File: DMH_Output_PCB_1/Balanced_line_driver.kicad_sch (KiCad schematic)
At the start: 12 parts, among them U10 NE5532, U9 NE5532

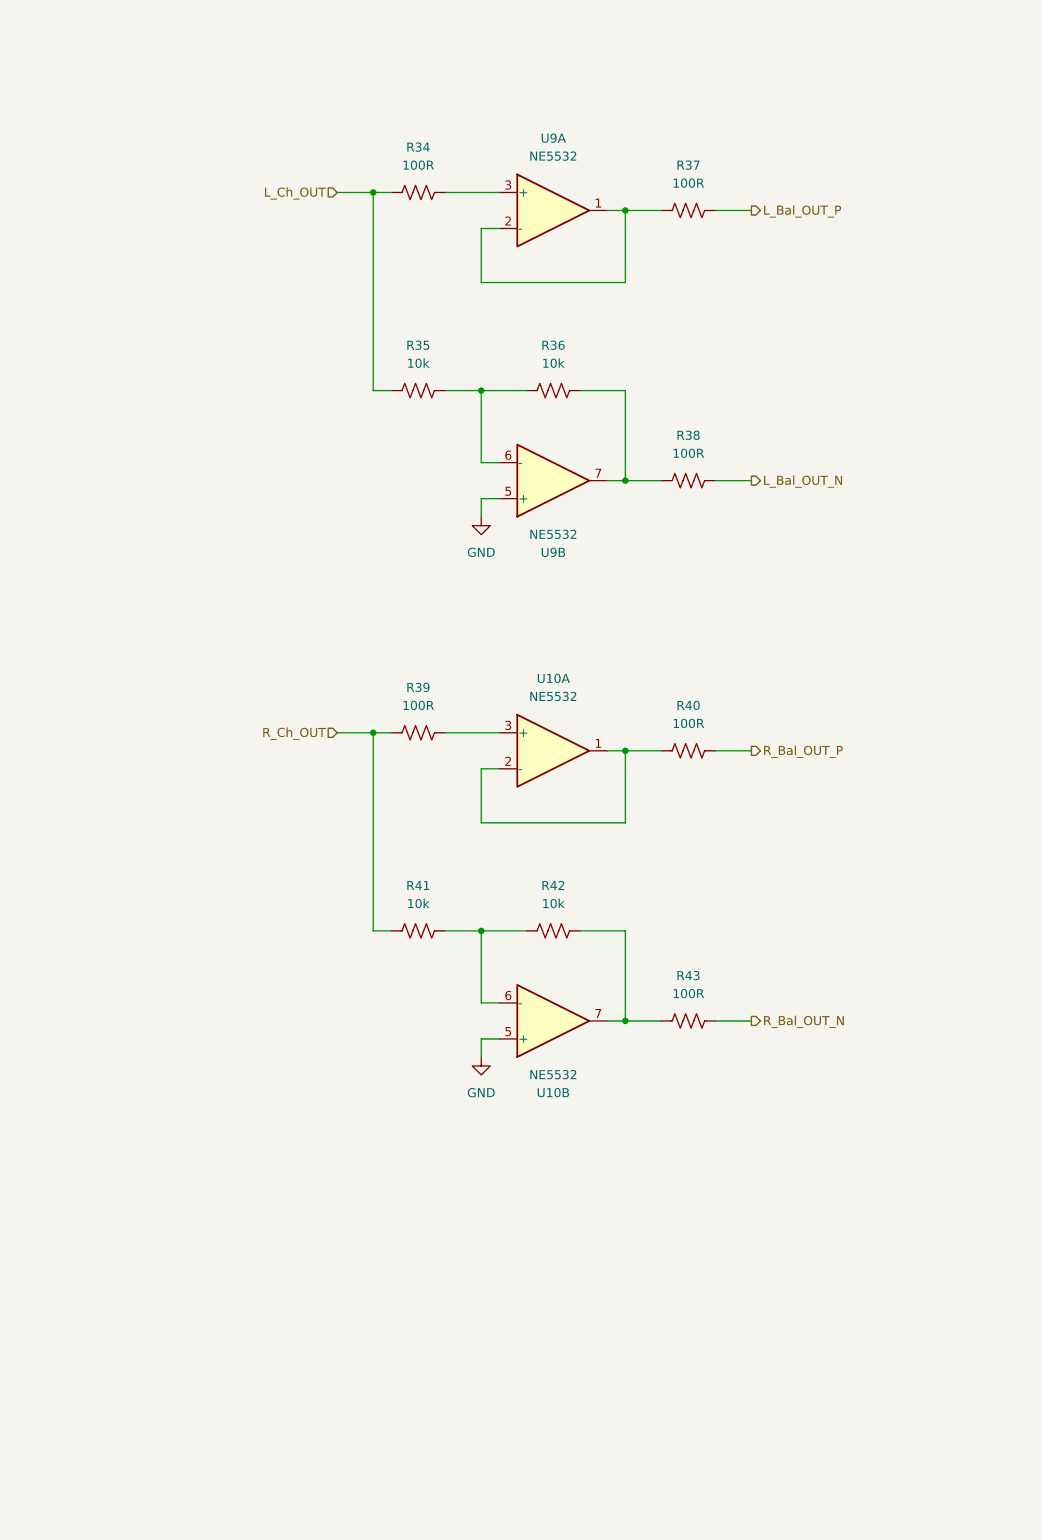
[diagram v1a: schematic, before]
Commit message: Changed balanced output for quasi-floating design
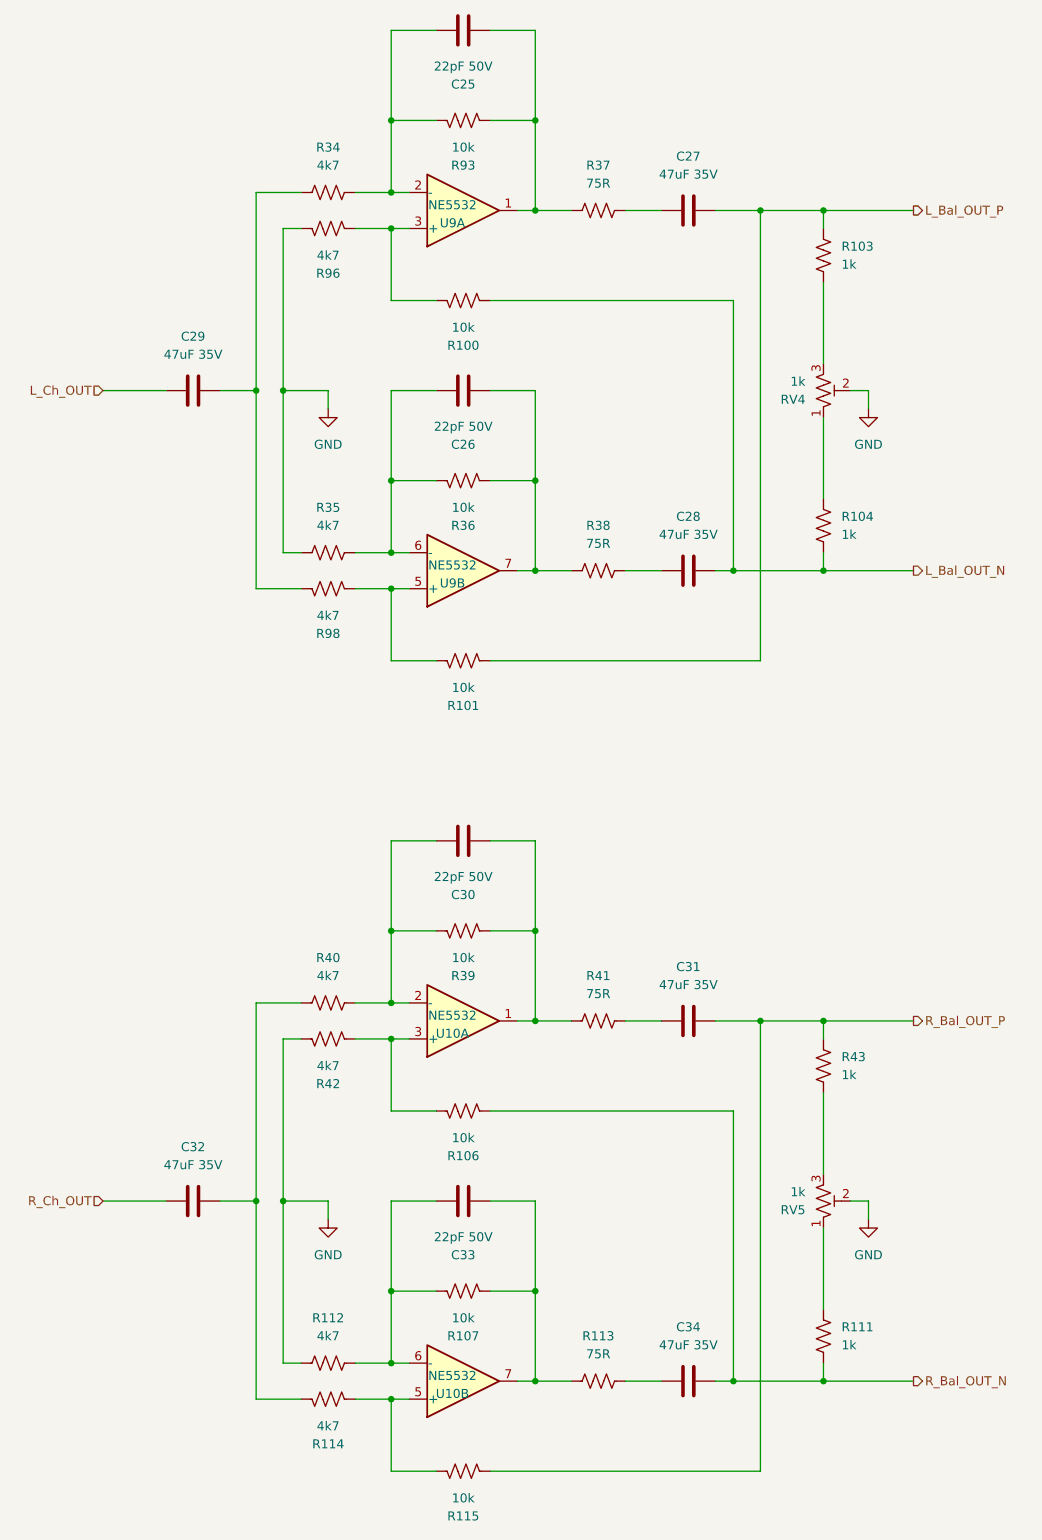
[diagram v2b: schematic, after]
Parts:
- added C25, C26, C30, C33: 22pF 50V, Capacitor_THT:C_Disc_D3.0mm_W2.0mm_P2.50mm, symbol Device:C
- added C27, C28, C29, C31, C32, C34: 47uF 35V, Capacitor_THT:C_Radial_D8.0mm_H11.5mm_P3.50mm, symbol Device:C
- added R100, R101, R106, R107, R115, R93: 10k, Resistor_THT:R_Axial_DIN0207_L6.3mm_D2.5mm_P7.62mm_Horizontal, symbol Device:R_US
- added R103, R104, R111: 1k, Resistor_THT:R_Axial_DIN0207_L6.3mm_D2.5mm_P7.62mm_Horizontal, symbol Device:R_US
- added R112, R114, R96, R98: 4k7, Resistor_THT:R_Axial_DIN0207_L6.3mm_D2.5mm_P7.62mm_Horizontal, symbol Device:R_US
- added R113: 75R, Resistor_THT:R_Axial_DIN0207_L6.3mm_D2.5mm_P7.62mm_Horizontal, symbol Device:R_US
- added RV4, RV5: 1k, Potentiometer_THT:Potentiometer_Bourns_3296W_Vertical, symbol Device:R_Potentiometer_Trim_US
- R34, R40: value 100R -> 4k7
- R35, R42: value 10k -> 4k7
- R37, R38: value 100R -> 75R
- R39: value 100R -> 10k
- R41: value 10k -> 75R
- R43: value 100R -> 1k
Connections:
- net GND: now also R35.1, R42.1, R112.1, R96.1, RV4.2, RV5.2; no longer U10.5 (+), U9.5 (+)
- net L_Bal_OUT_N: now also C28.2, R100.2, R104.1; no longer R38.2
- net L_Bal_OUT_P: now also C27.2, R101.2, R103.2; no longer R37.2
- net L_Ch_OUT: now also C29.1; no longer R34.1, R35.1
- net R_Bal_OUT_N: now also C34.2, R106.2, R111.1; no longer R43.2
- net R_Bal_OUT_P: now also R43.2, C31.2, R115.2; no longer R40.2
- net R_Ch_OUT: now also C32.1; no longer R39.1, R41.1
- net at U10.3 (+): now also R42.2, R106.1; no longer R39.2
- net at R35.2, R36.1, U9.6 (-): now also C26.1
- net at R36.2, R38.1, U9.7: now also C26.2
- net at U9.3 (+): now also R100.1, R96.2; no longer R34.2
- net at R37.1, U9.1: now also C25.2, R93.2; no longer U9.2 (-)
- new net: C33.1, R107.1, R112.2, U10.6 (-)
- new net: C33.2, R107.2, R113.1, U10.7
- new net: C31.1, R41.2
- new net: R104.2, RV4.1
- new net: R103.1, RV4.3
- new net: R101.1, R98.2, U9.5 (+)
- new net: C28.1, R38.2
- new net: C25.1, R34.2, R93.1, U9.2 (-)
- new net: C34.1, R113.2
- new net: C32.2, R114.1, R40.1
- new net: R114.2, R115.1, U10.5 (+)
- new net: C29.2, R34.1, R98.1
- new net: C30.1, R39.1, R40.2, U10.2 (-)
- new net: C30.2, R39.2, R41.1, U10.1
- new net: C27.1, R37.2
- new net: R43.1, RV5.3
- new net: R111.2, RV5.1
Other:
- moved on the sheet: R34, R35, R36, R37, R38, U9A, U9B

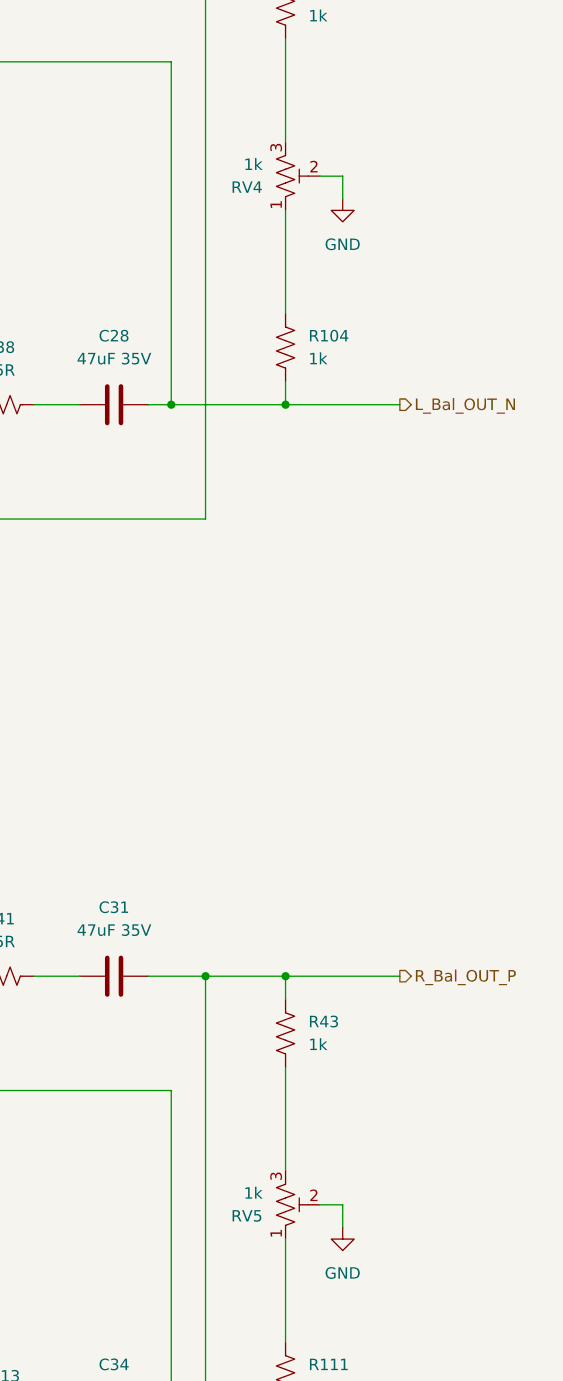
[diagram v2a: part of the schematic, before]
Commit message: Redesigned external input preamp
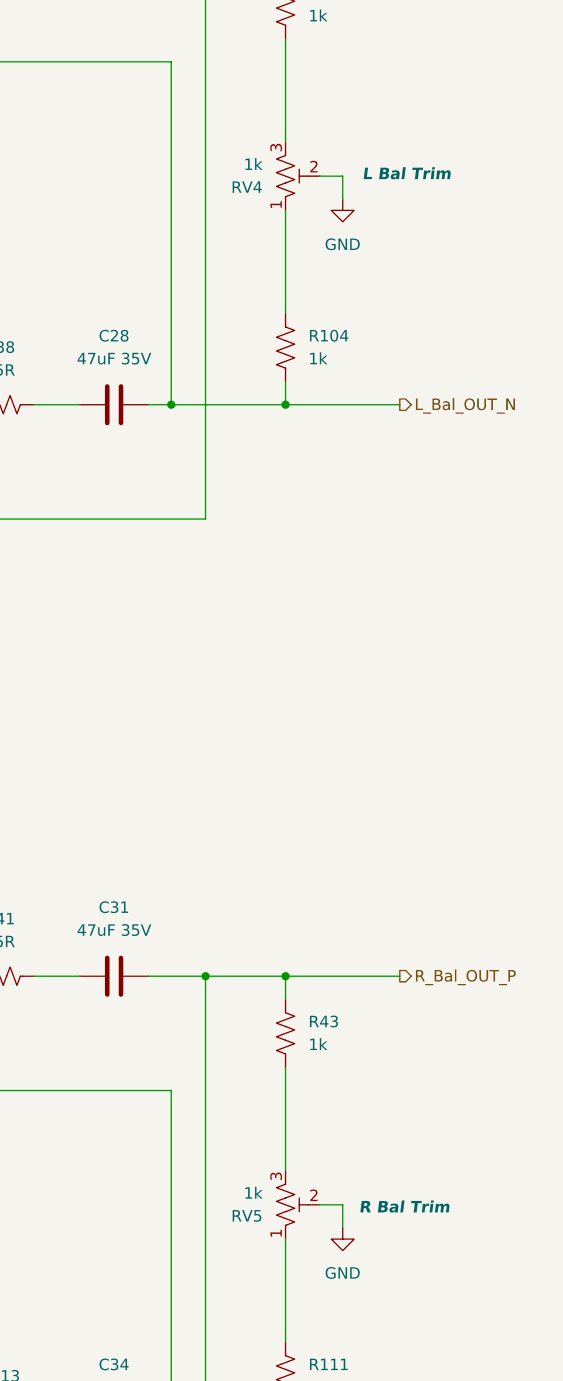
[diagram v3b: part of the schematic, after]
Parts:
- RV4: Function (none) -> L Bal Trim
- RV5: Function (none) -> R Bal Trim
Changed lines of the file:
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@@
 			)
 		)
-		(property "Function" ""
-			(at 152.4 76.2 0)
-			(effects
-				(font
-					(size 1.27 1.27)
+		(property "Function" "L Bal Trim"
+			(at 165.862 75.946 0)
+			(effects
+				(font
+					(size 1.27 1.27)
+					(thickness 0.254)
+					(bold yes)
+					(italic yes)
 				)
 			)
@@
 			)
 		)
-		(property "Function" ""
-			(at 152.4 190.5 0)
-			(effects
-				(font
-					(size 1.27 1.27)
-				)
-			)
+		(property "Function" "R Bal Trim"
+			(at 165.608 190.754 0)
+			(effects
+				(font
+					(size 1.27 1.27)
+					(thickness 0.254)
+					(bold yes)
+					(italic yes)
+				)
+			)
